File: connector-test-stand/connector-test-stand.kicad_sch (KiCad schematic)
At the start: 68 parts, among them J1 DVI-I_Dual_Link, J10 Conn_01x04_MountingPin, J2 Conn_01x02, J3 Conn_01x02, J4 Conn_01x05, J5 Conn_01x02, J6 Conn_01x03, J7 Conn_01x10, J8 Conn_01x04_MountingPin, J9 Conn_01x03, K1 G2RL-1-E, U1 REF5010AD, U2 INA333xxDGK, U3 P82B96, U4 SN65HVD11HD, U5 OPA333xxD, U6 PCF8574RGTR, U7 TBD62783A, U8 74LS540, U9 SN74LVC1G125DBV

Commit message: Fix power, add buffer
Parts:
- removed U1: REF5010AD, Package_SO:SOIC-8_3.9x4.9mm_P1.27mm, symbol Reference_Voltage:REF5010AD
- added C10, C11, C12, C13, C8, C9: C, symbol Device:C
- added J11: Conn_01x02, symbol Connector_Generic:Conn_01x02
- added R16: R, symbol Device:R
- added U1: REF5050AD, Package_SO:SOIC-8_3.9x4.9mm_P1.27mm, symbol Reference_Voltage:REF5050AD
- added U10: SN74LVC1G125DBV, Package_TO_SOT_SMD:SOT-23-5, symbol 74xGxx:SN74LVC1G125DBV
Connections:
- net VSSA is gone; now on net GND: U2.4 (V-), U5.4 (V-)
- net +12V: now also C1.1, J1.15 (GND), J1.C4 (HSYNC), U1.2 (Vin); no longer J10.3 (Pin_3)
- net +3.3V: now also C11.1, C13.1, C8.1, C9.1, U10.5 (VCC)
- net GND: now also C10.2, C11.2, C12.2, C13.2, C8.2, C9.2, J11.1 (Pin_1), R16.2, U1.4 (GND), U10.1, U10.3 (GND)
- net N2O valve servo PWM pin: now also R16.1, U10.2; no longer J6.1 (Pin_1)
- net VDD: now also J10.3 (Pin_3), C10.1, J11.2 (Pin_2)
- net VDDA: now also J1.9 (D1-), C12.1
- net at R1.2: now also U1.5 (Trim/NR)
- net at C2.1, J4.1 (Pin_1), R6.1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: now also U1.6 (Vout)
- removed net STRAIN_GAUGE_POWER_SUPPLY: C1.1, J1.9 (D1-)
- new net: J6.1 (Pin_1), U10.4
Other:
- note added: "AGM lead battery 12V"
- note added: "Connect signal light and other utilities"
- note added: "Starter high current connector"

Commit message: Add first revision of board for the test stand connector
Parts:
- removed J9: Conn_01x03, symbol Connector_Generic:Conn_01x03
- added H1, H2, H3, H4: MountingHole_Pad, MountingHole:MountingHole_3.2mm_M3_Pad_Via, symbol Mechanical:MountingHole_Pad
- added J11: Conn_01x03_MountingPin, Connector_JST:JST_PH_S3B-PH-SM4-TB_1x03-1MP_P2.00mm_Horizontal, symbol Connector_Generic_MountingPin:Conn_01x03_MountingPin
- C1: renamed from C6; footprint (none) -> Capacitor_SMD:C_0805_2012Metric
- C10: renamed from C7; footprint (none) -> Capacitor_SMD:CP_Elec_10x10
- C11, C2: footprint (none) -> Capacitor_SMD:C_0805_2012Metric
- C12: renamed from C3; footprint (none) -> Capacitor_SMD:C_0805_2012Metric
- C13: renamed from C4; footprint (none) -> Capacitor_SMD:C_0805_2012Metric
- C3: renamed from C8; footprint (none) -> Capacitor_SMD:C_0805_2012Metric
- C4: renamed from C9; footprint (none) -> Capacitor_SMD:C_0805_2012Metric
- C5: renamed from C12; footprint (none) -> Capacitor_SMD:C_0805_2012Metric
- C6: renamed from C13; footprint (none) -> Capacitor_SMD:C_0805_2012Metric
- C7: renamed from C1; footprint (none) -> Capacitor_SMD:C_0805_2012Metric
- C8: renamed from C5; footprint (none) -> Capacitor_SMD:C_0805_2012Metric
- C9: renamed from C10; footprint (none) -> Capacitor_SMD:C_0805_2012Metric
- D1: renamed from D3; footprint (none) -> Diode_SMD:D_SMB
- F1: footprint (none) -> Fuse:Fuseholder_Cylinder-5x20mm_Bulgin_FX0456_Vertical_Closed
- F2, F3, F4, F5, F6, F7, F8, F9: footprint (none) -> Fuse:Fuseholder_Clip-5x20mm_Schurter_CQM_Inline_P20.60x5.00mm_D1.00mm_Horizontal
- FB1: renamed from FB6; footprint (none) -> Inductor_SMD:L_0805_2012Metric
- FB2: renamed from FB7; footprint (none) -> Inductor_SMD:L_0805_2012Metric
- FB3: renamed from FB1; footprint (none) -> Inductor_SMD:L_0805_2012Metric
- FB4: renamed from FB2; footprint (none) -> Inductor_SMD:L_0805_2012Metric
- FB5: renamed from FB3; footprint (none) -> Inductor_SMD:L_0805_2012Metric
- FB6: renamed from FB4; footprint (none) -> Inductor_SMD:L_0805_2012Metric
- FB7: renamed from FB5; footprint (none) -> Inductor_SMD:L_0805_2012Metric
- J1: renamed from J5; footprint (none) -> Connector_AMASS:AMASS_XT30PW-M_1x02_P2.50mm_Horizontal
- J10, J9: renamed from J8; footprint (none) -> Connector_JST:JST_PH_S4B-PH-SM4-TB_1x04-1MP_P2.00mm_Horizontal
- J12: renamed from J1; footprint (none) -> Connector_Video:DVI-I_Molex_74320-1004_Horizontal
- J2, J3: footprint (none) -> TerminalBlock:TerminalBlock_Altech_AK300-2_P5.00mm
- J4: footprint (none) -> TerminalBlock_Altech:Altech_AK100_1x05_P5.00mm
- J5: renamed from J10; footprint (none) -> Connector_JST:JST_PH_S4B-PH-SM4-TB_1x04-1MP_P2.00mm_Horizontal
- J6: renamed from J11; footprint (none) -> Connector_AMASS:AMASS_XT30PW-M_1x02_P2.50mm_Horizontal
- J7: renamed from J6; footprint (none) -> TerminalBlock:TerminalBlock_Altech_AK300-3_P5.00mm
- J8: renamed from J7; footprint (none) -> TerminalBlock_Altech:Altech_AK100_1x10_P5.00mm
- R10: renamed from R6; footprint (none) -> Resistor_SMD:R_0805_2012Metric
- R11: renamed from R7; footprint (none) -> Resistor_SMD:R_0805_2012Metric
- R12: renamed from R14; footprint (none) -> Resistor_SMD:R_0805_2012Metric
- R13: renamed from R15; footprint (none) -> Resistor_SMD:R_0805_2012Metric
- R14: renamed from R12; footprint (none) -> Resistor_SMD:R_0805_2012Metric
- R15: renamed from R13; footprint (none) -> Resistor_SMD:R_0805_2012Metric
- R16: renamed from R5; footprint (none) -> Resistor_SMD:R_0805_2012Metric
- R17: renamed from R3; footprint (none) -> Resistor_SMD:R_0805_2012Metric
- R18: renamed from R4; footprint (none) -> Resistor_SMD:R_0805_2012Metric
- R7: renamed from R2; footprint (none) -> Resistor_SMD:R_0805_2012Metric
- R8: renamed from R1; footprint (none) -> Resistor_SMD:R_0805_2012Metric
- R9: renamed from R16; footprint (none) -> Resistor_SMD:R_0805_2012Metric
- RV1: renamed from RV4; footprint (none) -> Potentiometer_THT:Potentiometer_Bourns_3266W_Vertical
- RV2: renamed from RV1; footprint (none) -> Potentiometer_THT:Potentiometer_Bourns_3266W_Vertical
- RV3: renamed from RV2; footprint (none) -> Potentiometer_THT:Potentiometer_Bourns_3266W_Vertical
- RV4: renamed from RV3; footprint (none) -> Potentiometer_THT:Potentiometer_Bourns_3266W_Vertical
- U1: renamed from U6; footprint PCF8574RGTR:QFN50P300X300X100-17N -> th:QFN50P300X300X100-17N
- U4: renamed from U8; footprint (none) -> Package_SO:SO-20_12.8x7.5mm_P1.27mm
- U7: footprint (none) -> Package_SO:SOP-18_7x12.5mm_P1.27mm
- U9: renamed from U3; footprint (none) -> Package_SO:SOIC-8_3.9x4.9mm_P1.27mm
- renumbered D1 to D2, D2 to D3, R8 to R1, R9 to R2, R10 to R3, R8 to R4, R11 to R5, R9 to R6, U4 to U10, U1 to U3, U10 to U6, U9 to U8
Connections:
- net +3.3V: now also J11.2 (Pin_2)
- net +BATT: now also J1.2 (Pin_2); no longer J1.1 (Pin_1)
- net GND: now also J1.1 (Pin_1), J8.1 (Pin_1), H1.1, H2.1, H3.1, H4.1, J11.3 (Pin_3), J11.MP (MountPin); no longer J1.2 (Pin_2), J8.10 (Pin_10)
- net VDD: now also J8.10 (Pin_10); no longer J8.1 (Pin_1)
- net at R12.2, R13.2, U8.4: now also J11.1 (Pin_1)
- net at F2.2: now also J8.9 (Pin_9); no longer J8.2 (Pin_2)
- net at F6.2: now also J8.5 (Pin_5); no longer J8.6 (Pin_6)
- net at F5.2: now also J8.6 (Pin_6); no longer J8.5 (Pin_5)
- net at F8.2: now also J8.3 (Pin_3); no longer J8.8 (Pin_8)
- net at F4.2: now also J8.7 (Pin_7); no longer J8.4 (Pin_4)
- net at F3.2: now also J8.8 (Pin_8); no longer J8.3 (Pin_3)
- net at F7.2: now also J8.4 (Pin_4); no longer J8.7 (Pin_7)
- net at F9.2: now also J8.2 (Pin_2); no longer J8.9 (Pin_9)
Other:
- moved on the sheet: J1

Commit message: change strain power supply
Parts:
- added C14: C, Capacitor_SMD:C_0805_2012Metric, symbol Device:C
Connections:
- net +3.3V: now also C5.1, U2.7 (V+), U5.7 (V+), C14.1
- net GND: now also J12.9 (D1-), C14.2
- removed net VDDA: C5.1, J12.9 (D1-), U2.7 (V+), U5.7 (V+)

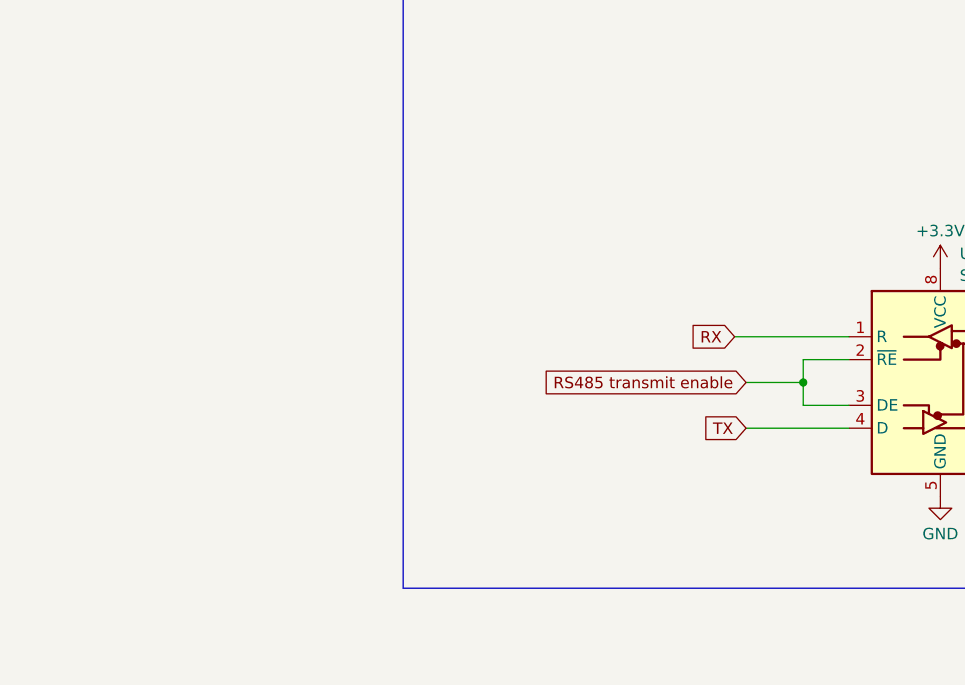
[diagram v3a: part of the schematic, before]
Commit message: Fix uart connection, add crossing and enable negation
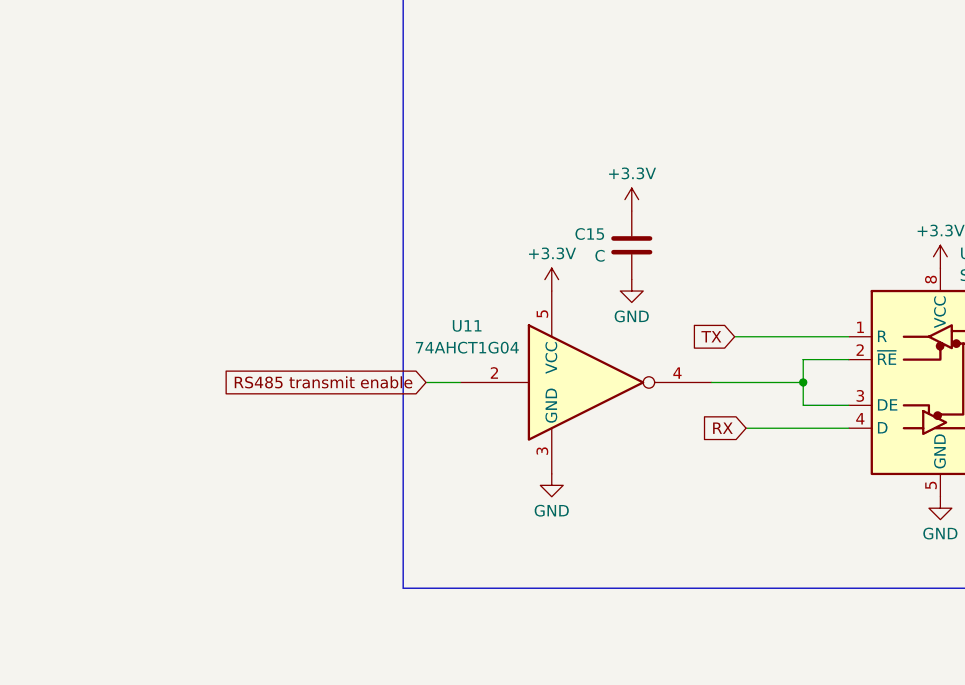
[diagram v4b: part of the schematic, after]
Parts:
- added C15: C, Capacitor_SMD:C_0805_2012Metric, symbol Device:C
- added U11: 74AHCT1G04, Package_TO_SOT_SMD:SOT-23-5, symbol 74xGxx:74AHCT1G04
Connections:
- net +3.3V: now also C15.1, U11.5 (VCC)
- net GND: now also C15.2, U11.3 (GND)
- net RS485 transmit enable: now also U11.2; no longer U10.2 (~{RE}), U10.3 (DE)
- net RX: now also U10.4 (D); no longer U10.1 (R)
- net TX: now also U10.1 (R); no longer U10.4 (D)
- new net: U10.2 (~{RE}), U10.3 (DE), U11.4

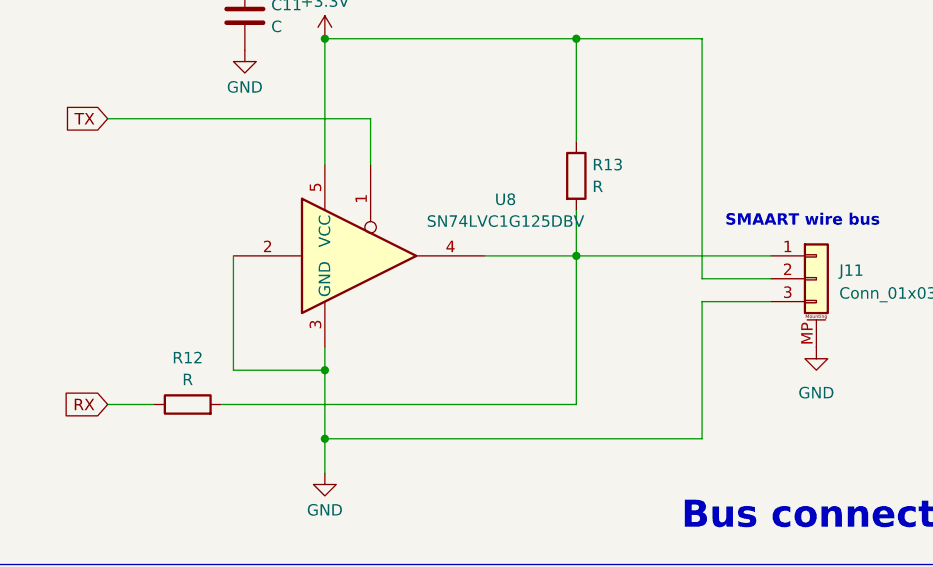
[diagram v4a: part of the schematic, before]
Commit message: Add values for SMAART wire conevrter and safety rezistor
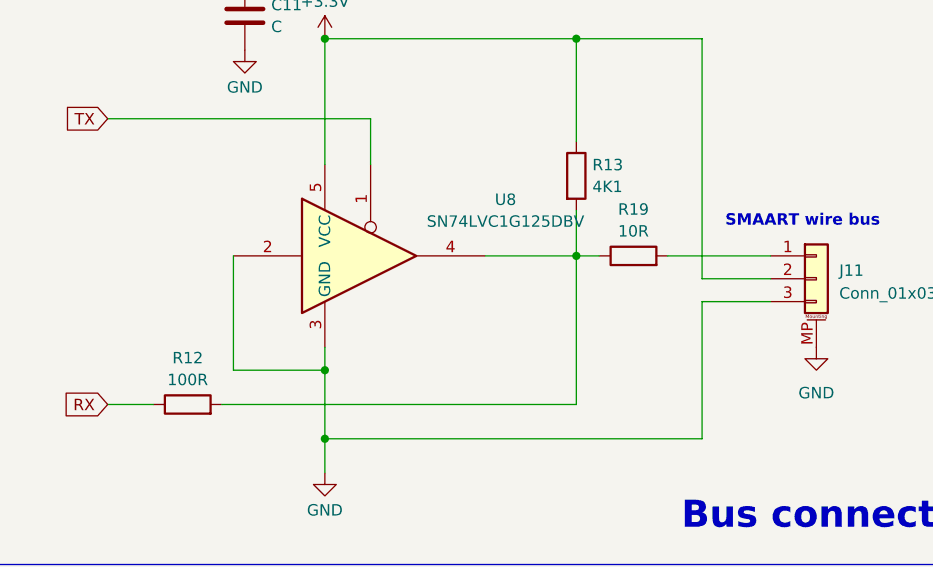
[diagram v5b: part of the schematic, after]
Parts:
- added R19: 10R, Resistor_SMD:R_0805_2012Metric, symbol Device:R
- R12: value R -> 100R
- R13: value R -> 4K1
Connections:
- net at R12.2, R13.2, U8.4: now also R19.1; no longer J11.1 (Pin_1)
- new net: J11.1 (Pin_1), R19.2
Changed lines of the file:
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@@
 	(wire
 		(pts
-			(xy 270.51 123.19) (xy 292.1 123.19)
-		)
-		(stroke
-			(width 0)
-			(type default)
-		)
-	)
-	(wire
-		(pts
 			(xy 505.46 125.73) (xy 505.46 128.27)
 		)
@@
 	(wire
 		(pts
+			(xy 270.51 123.19) (xy 273.05 123.19)
+		)
+		(stroke
+			(width 0)
+			(type default)
+		)
+	)
+	(wire
+		(pts
 			(xy 36.83 353.06) (xy 36.83 363.22)
 		)
@@
 	(wire
 		(pts
+			(xy 280.67 123.19) (xy 292.1 123.19)
+		)
+		(stroke
+			(width 0)
+			(type default)
+		)
+	)
+	(wire
+		(pts
 			(xy 480.06 77.47) (xy 497.84 77.47)
 		)
@@
 			)
 		)
-		(property "Value" "R"
+		(property "Value" "100R"
 			(at 227.33 136.9638 90)
 			(effects
@@
 			)
 		)
-		(property "Value" "R"
+		(property "Value" "4K1"
 			(at 272.288 115.5121 0)
 			(effects
@@
 					(unit 1)
 				)
+			)
+		)
+	)
+	(symbol
+		(lib_id "Device:R")
+		(at 276.86 123.19 90)
+		(unit 1)
+		(exclude_from_sim no)
+		(in_bom yes)
+		(on_board yes)
+		(dnp no)
+		(fields_autoplaced yes)
+		(property "Reference" "R19"
+			(at 276.86 118.0295 90)
+			(effects
+				(font
+					(size 1.27 1.27)
+				)
+			)
+		)
+		(property "Value" "10R"
+			(at 276.86 120.4538 90)
+			(effects
+				(font
+					(size 1.27 1.27)
+				)
+			)
+		)
+		(property "Footprint" "Resistor_SMD:R_0805_2012Metric"
+			(at 276.86 124.968 90)
+			(effects
+				(font
+					(size 1.27 1.27)
+				)
+				(hide yes)
+			)
+		)
+		(property "Datasheet" "~"
+			(at 276.86 123.19 0)
+			(effects
+				(font
+					(size 1.27 1.27)
+				)
+				(hide yes)
+			)
+		)
+		(property "Description" "Resistor"
+			(at 276.86 123.19 0)
+			(effects
+				(font
+					(size 1.27 1.27)
+				)
+				(hide yes)
+			)
+		)
+		(pin "1"
+		)
+		(pin "2"
+		)
+		(instances
+			(project "connector-test-stand"
+				(path "/6efdf98c-bc7d-454c-9186-483ddeb32201"
+					(reference "R19")
+					(unit 1)
+				)

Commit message: Rework connector test stand board
* Add values for elements
* Rework power supply
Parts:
- removed C7: C, Capacitor_SMD:C_0805_2012Metric, symbol Device:C
- removed R7, R8: R, Resistor_SMD:R_0805_2012Metric, symbol Device:R
- removed RV2: R_Potentiometer, Potentiometer_THT:Potentiometer_Bourns_3266W_Vertical, symbol Device:R_Potentiometer
- removed U3: REF5050AD, Package_SO:SOIC-8_3.9x4.9mm_P1.27mm, symbol Reference_Voltage:REF5050AD
- added C7: 1000uF 16V, Capacitor_SMD:CP_Elec_10x10, symbol Device:C_Polarized
- added R20, R21: 10R thick film, Resistor_SMD:R_0805_2012Metric, symbol Device:R
- added U12: CDSOT236-0504C, Package_TO_SOT_SMD:SOT-23-6, symbol Power_Protection:CDSOT236-0504C
- added U13: MCP1501-40xSN, Package_SO:SOIC-8_3.9x4.9mm_P1.27mm, symbol Reference_Voltage:MCP1501-40xSN
- C1, C12, C13, C14, C15, C2, C3, C4, C5, C6, C8, C9: value C -> 100nF
- C10: value C_Polarized -> 1000uF 16V
- R10, R11: value R -> 10K 1%
- R14, R15, R9: value R -> 10K
- R17, R18: value R -> 330R
- RV1, RV4: value R_Potentiometer -> 1K
- RV3: value R_Potentiometer -> 12K
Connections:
- net +12V is gone; now on net +5V: C12.1, J12.15 (GND), J12.C4 (HSYNC), R17.1, R18.1, U9.8 (VCC)
- net +3.3V is gone; now on net +5V: C11.1, C13.1, C14.1, C15.1, C3.1, C4.1, C5.1, C6.1, J11.2 (Pin_2), J12.14 (+5V), J12.18 (D0+), J12.C2 (Green), J5.2 (Pin_2), R1.1, R13.1, R14.1, R15.1, R3.1, R5.1, U1.1 (VCC), U10.8 (VCC), U11.5 (VCC), U2.7 (V+), U4.20 (VCC), U5.7 (V+), U6.5 (VCC), U8.5 (VCC)
- net GND: now also C7.2, U12.2 (VN), U13.2 (GND), U13.4 (GND), U13.5 (GND), U13.6 (GND)
- net RS485 bus A: now also R20.2, U12.1 (IO1), U12.6 (IO4); no longer R16.1, U10.7 (B)
- net RS485 bus B: now also R21.2, U12.3 (IO2), U12.4 (IO3); no longer R16.2, U10.6 (A)
- net at J4.1 (Pin_1), R10.1: now also U13.7 (OUT), U13.8 (FB); no longer C2.1
- net +5V: now reaches J9.2 (Pin_2)
- net +5V: now also C2.1, J10.2 (Pin_2), C7.1, U12.5 (VP), U13.1 (VDD), U13.3 (~{SHDN})
- new net: R16.2, R21.1, U10.6 (A)
- new net: R16.1, R20.1, U10.7 (B)
- no-connect marks 7 -> 4
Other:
- moved on the sheet: C12, C13, C14, C15, C5, D2, D3, H1, H2, H3, H4, R14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

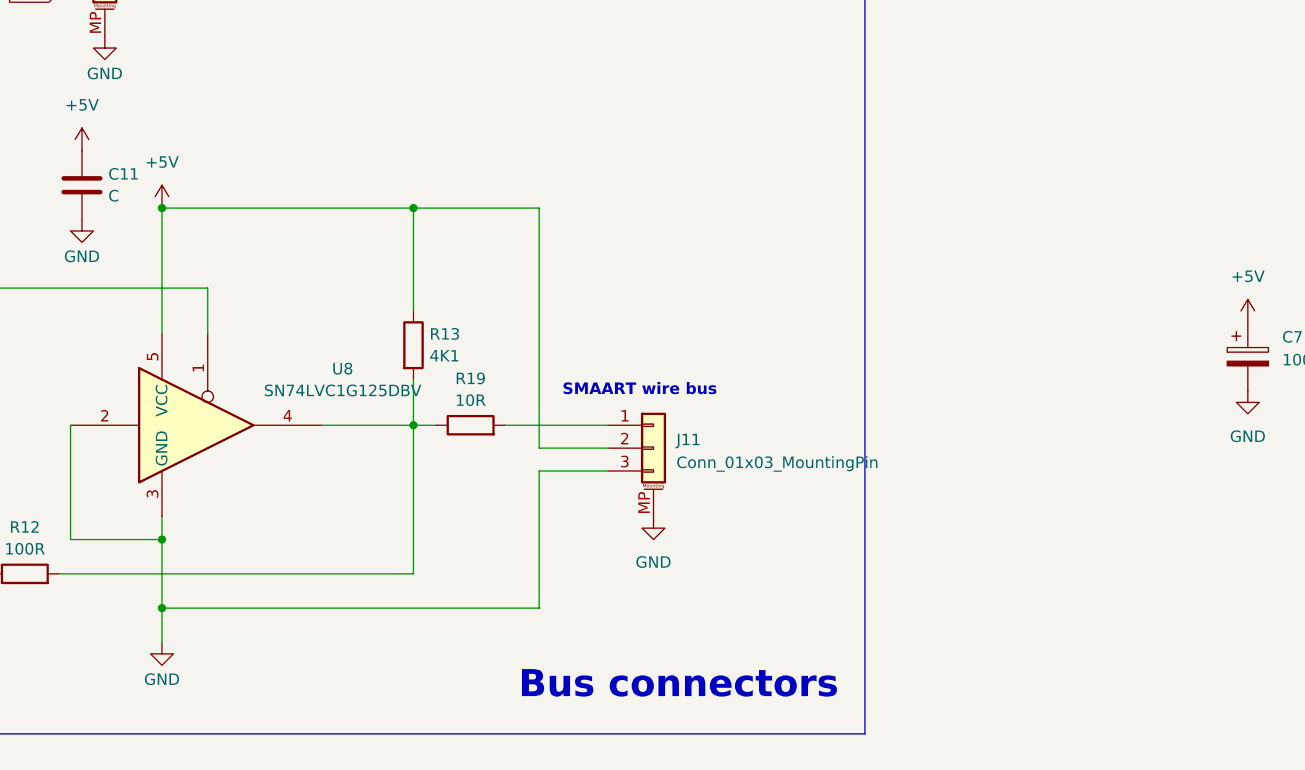
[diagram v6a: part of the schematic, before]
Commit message: Rework connector test stand
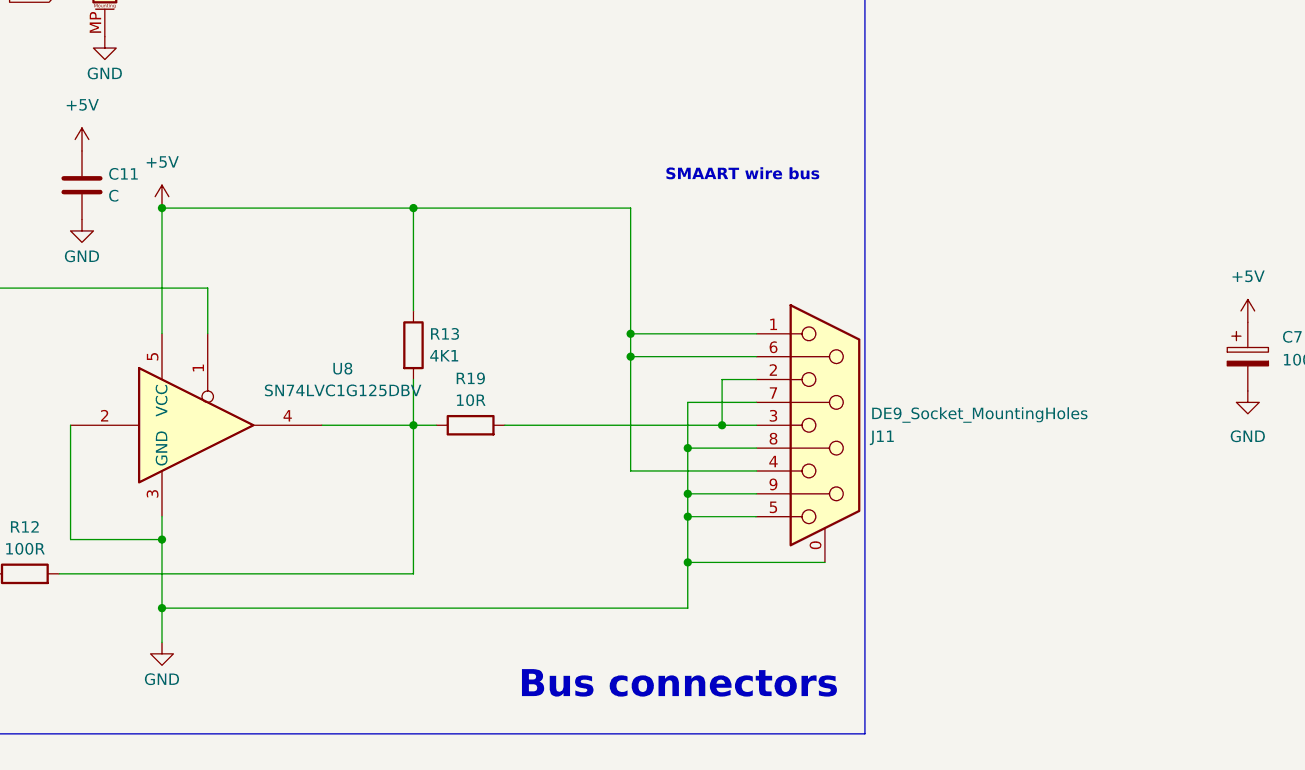
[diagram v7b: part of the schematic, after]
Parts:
- removed J11: Conn_01x03_MountingPin, Connector_JST:JST_PH_S3B-PH-SM4-TB_1x03-1MP_P2.00mm_Horizontal, symbol Connector_Generic_MountingPin:Conn_01x03_MountingPin
- added J11: DE9_Socket_MountingHoles, Connector_Dsub:DSUB-9_Socket_Horizontal_P2.77x2.84mm_EdgePinOffset9.90mm_Housed_MountingHolesOffset11.32mm, symbol Connector:DE9_Socket_MountingHoles
- J8: footprint TerminalBlock_Altech:Altech_AK100_1x10_P5.00mm -> TerminalBlock_4Ucon:TerminalBlock_4Ucon_1x10_P3.50mm_Horizontal
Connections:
- net +5V: now also J11.1, J11.4, J11.6
- net GND: now also J11.0 (PAD), J11.5, J11.7, J11.8, J11.9
- net at R19.2: now also J11.2, J11.3
